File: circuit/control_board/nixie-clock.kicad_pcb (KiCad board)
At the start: 2 copper layers, 102.4 x 50.8 mm, 45 parts, among them IC1 ATMEGA328-P, P1 CONN_2, P10 CONN_2, P2 CONN_2, P3 CONN_4, P4 CONN_4, P5 CONN_8, P6 CONN_12, P7 CONN_2, P8 CONN_2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

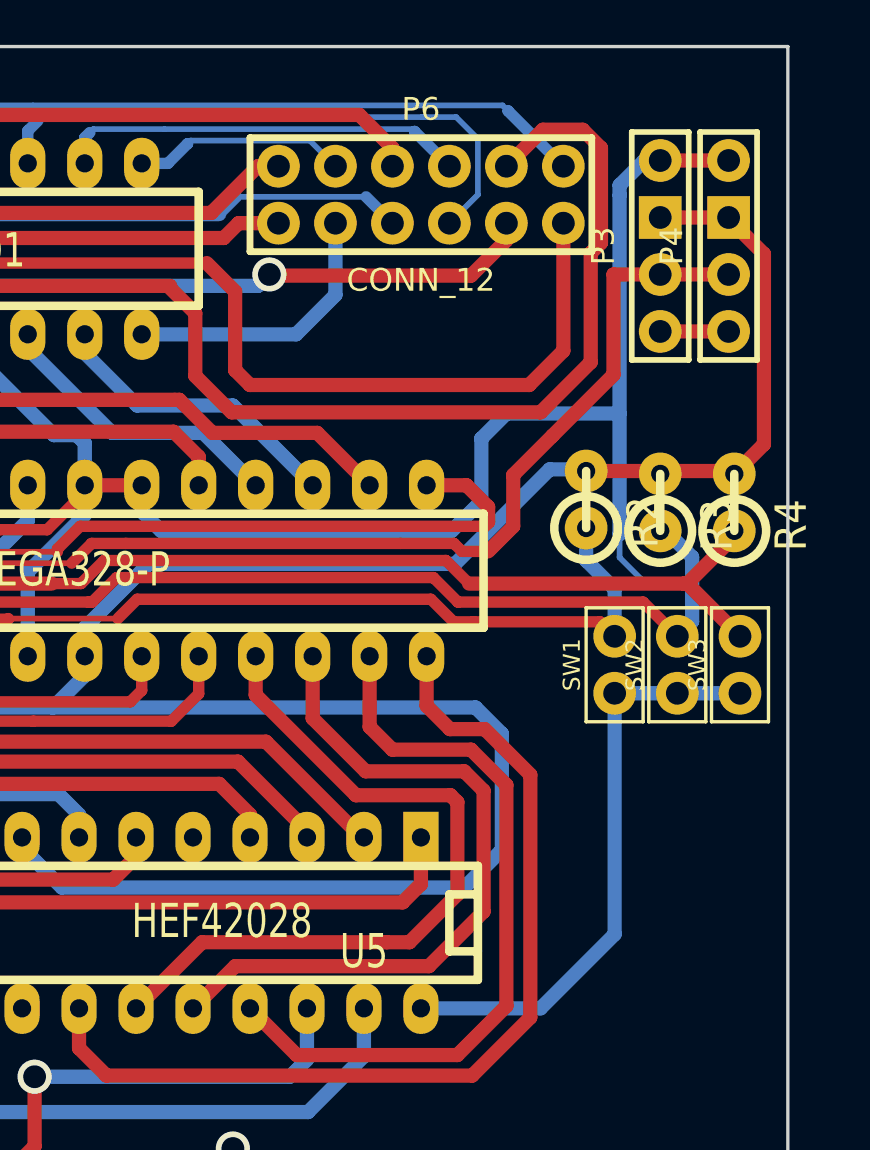
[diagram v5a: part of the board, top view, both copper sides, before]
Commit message: Control board: Fix the missing net
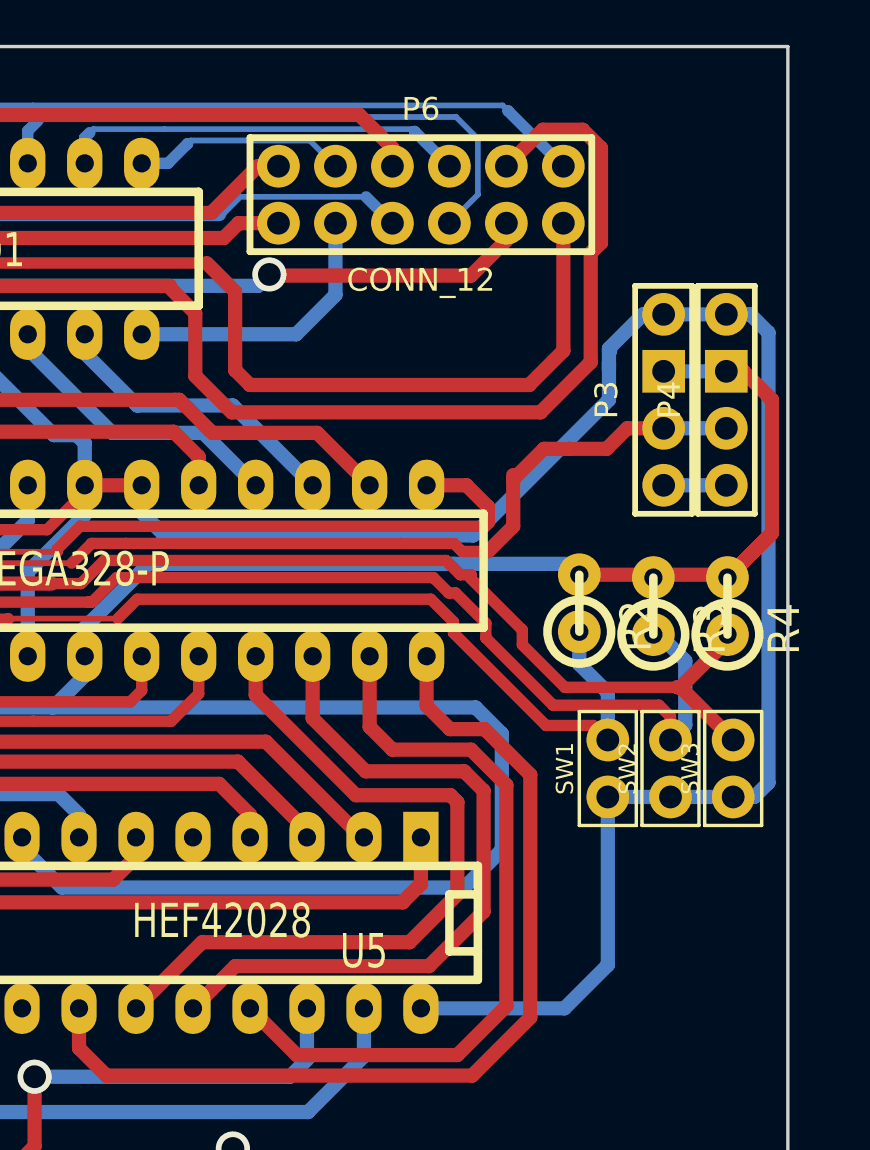
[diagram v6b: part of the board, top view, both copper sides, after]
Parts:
- moved P3 6.86 mm to (196.0, 94.5)
- moved P4 6.86 mm to (198.8, 94.5)
- moved R2 4.63 mm to (192.2, 103.6)
- moved R3 4.63 mm to (195.5, 103.7)
- moved R4 4.63 mm to (198.8, 103.7)
- moved SW1 4.63 mm to (193.5, 110.9)
- moved SW2 4.63 mm to (196.3, 110.9)
- moved SW3 4.63 mm to (199.1, 110.9)
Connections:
- P4 pad 1: Bluetooth /FTDIRx -> Bluetooth/FTDI Rx
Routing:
- net Bluetooth/FTDI Tx: track 56.2 -> 50.7 mm
- net GND: track 328.4 -> 332.5 mm
- net Adjust button: track 43.0 -> 45.6 mm
- net Mode button: track 53.0 -> 55.3 mm
- net Search button: track 37.2 -> 39.1 mm

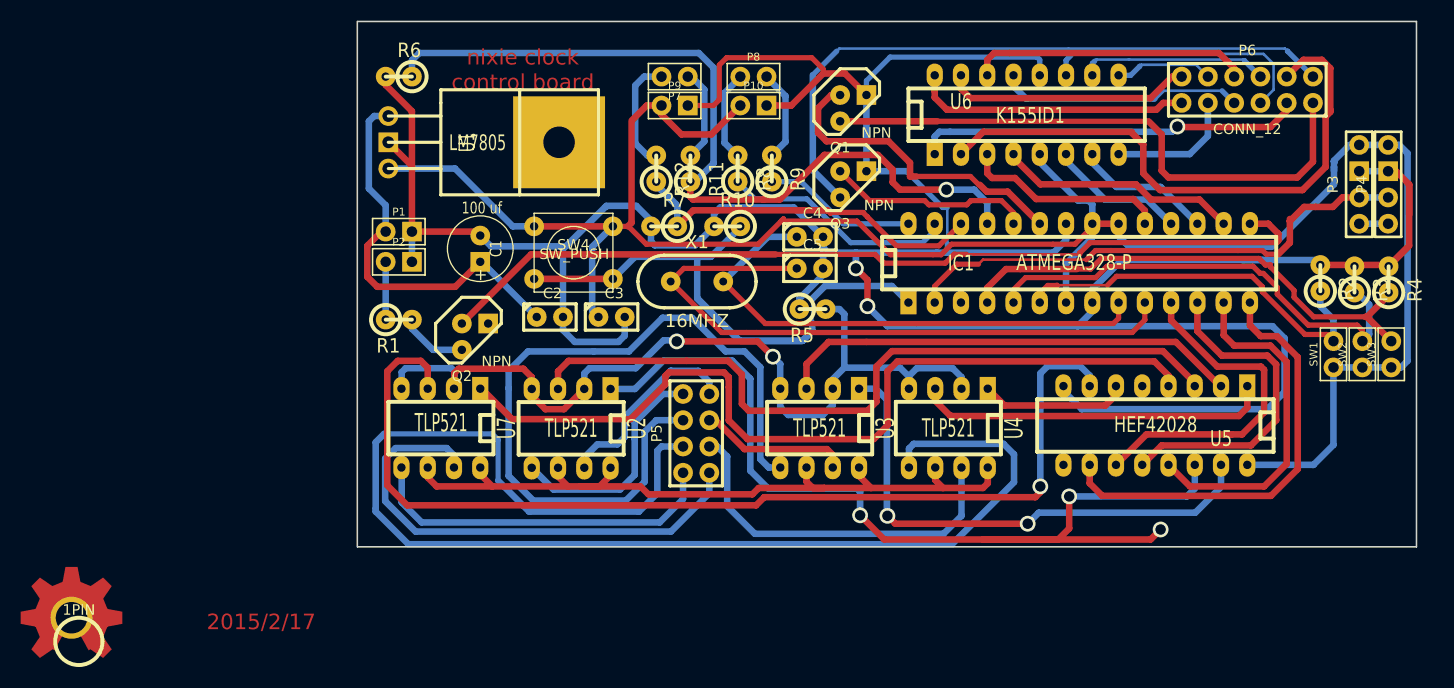
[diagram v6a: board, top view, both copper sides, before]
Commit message: Control board: Fix the FTDI Rx net and optimize some route
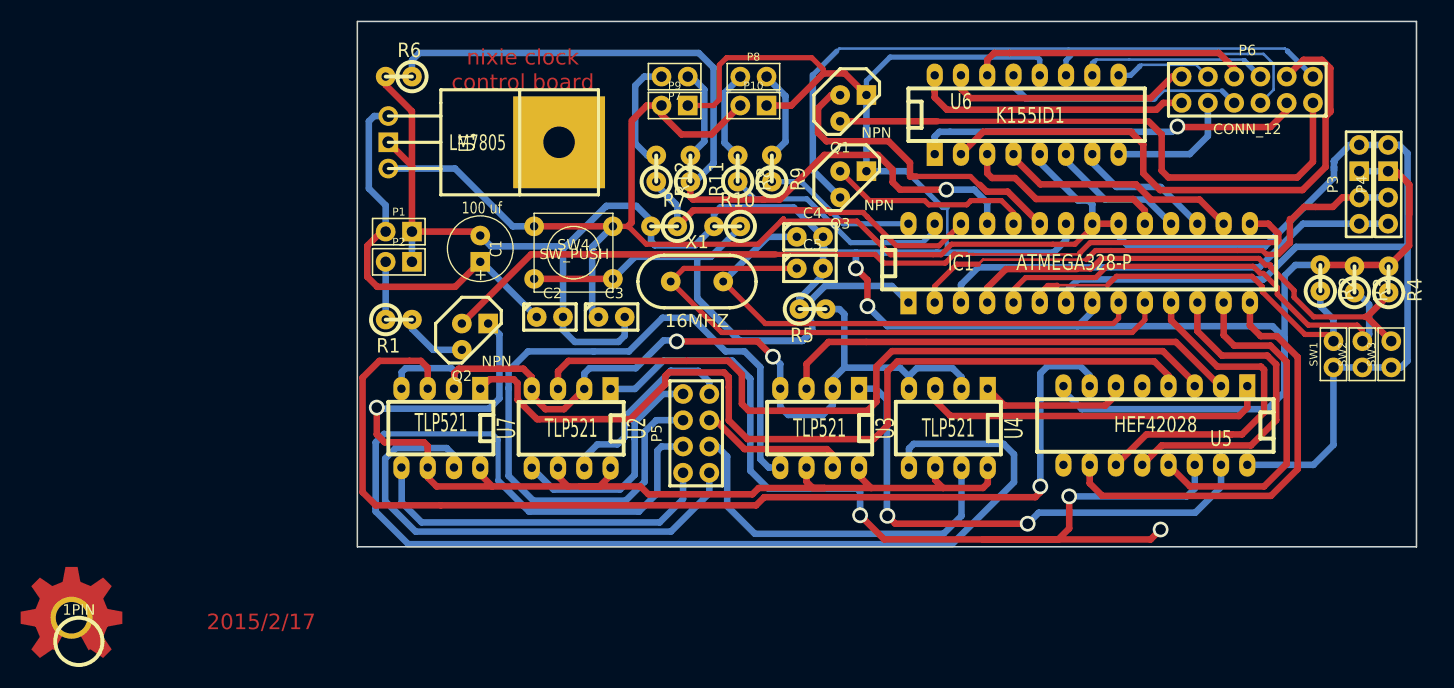
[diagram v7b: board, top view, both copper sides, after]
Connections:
- P3 pad 1: Bluetooth /FTDIRx -> Bluetooth/FTDI Rx
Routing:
- net Bluetooth/FTDI Rx: track 0.00 -> 45.5 mm
- net Net-(Q2-Pad1): track 74.6 -> 105.6 mm, vias 0 -> 1
- net 5V: track 212.5 -> 237.6 mm
- net GND: track 332.5 -> 321.0 mm
- net Net-(U5-Pad7): track 100.1 -> 104.9 mm
- net Bluetooth /FTDIRx: track 2.79 -> 0.00 mm
- net Net-(U5-Pad4): track 83.4 -> 85.1 mm

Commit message: Control board: Optimize the route
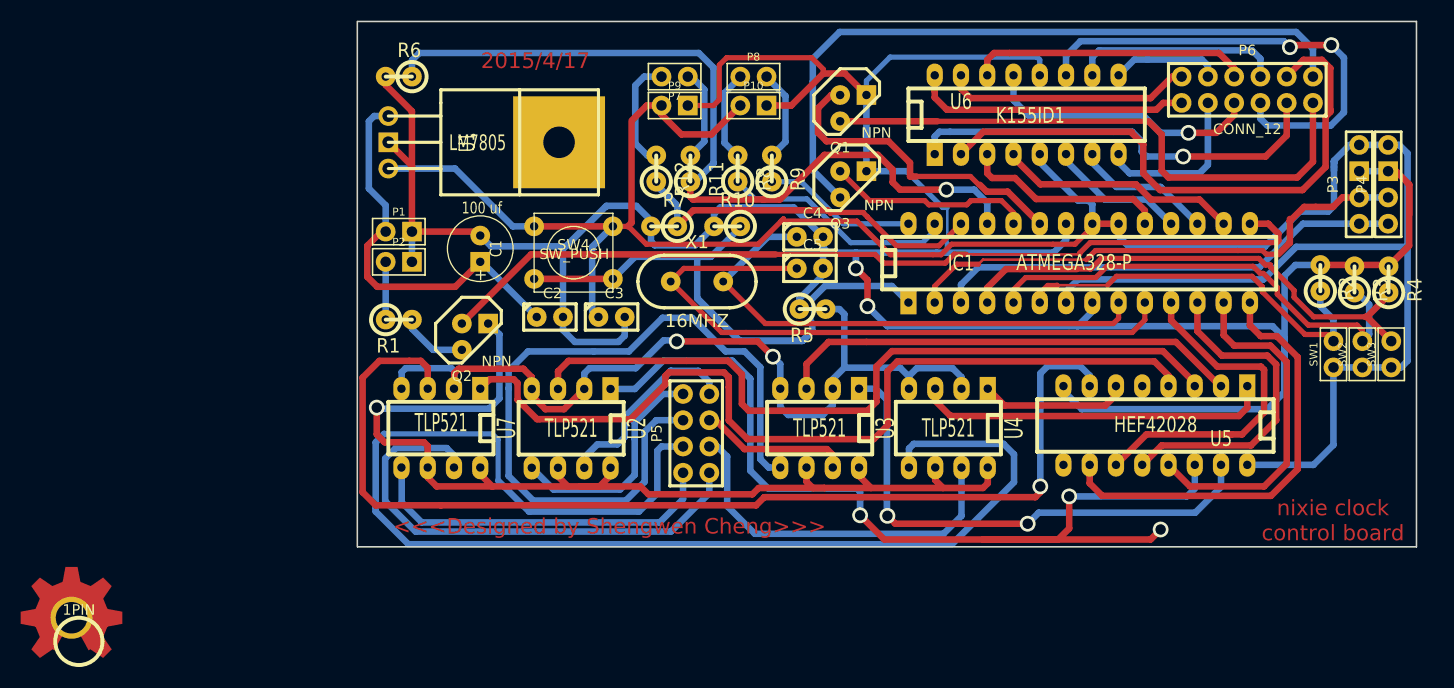
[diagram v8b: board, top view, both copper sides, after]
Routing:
- net Net-(P6-Pad7): track 27.9 -> 48.8 mm, vias 0 -> 2
- net Net-(P6-Pad5): track 39.5 -> 28.0 mm, vias 0 -> 1
- net Net-(P6-Pad9): track 37.6 -> 42.3 mm
- net Net-(P6-Pad12): track 63.5 -> 67.3 mm
- net Net-(P6-Pad3): track 12.6 -> 16.2 mm
- net Net-(P6-Pad8): track 19.4 -> 22.6 mm
- net 5V: track 237.6 -> 239.7 mm
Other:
- board text added: "2015/4/17"
- board text added: "<<<Designed by Shengwen Cheng>>>"
- board text removed: "2015/2/17"
